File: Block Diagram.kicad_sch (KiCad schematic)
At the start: 0 parts

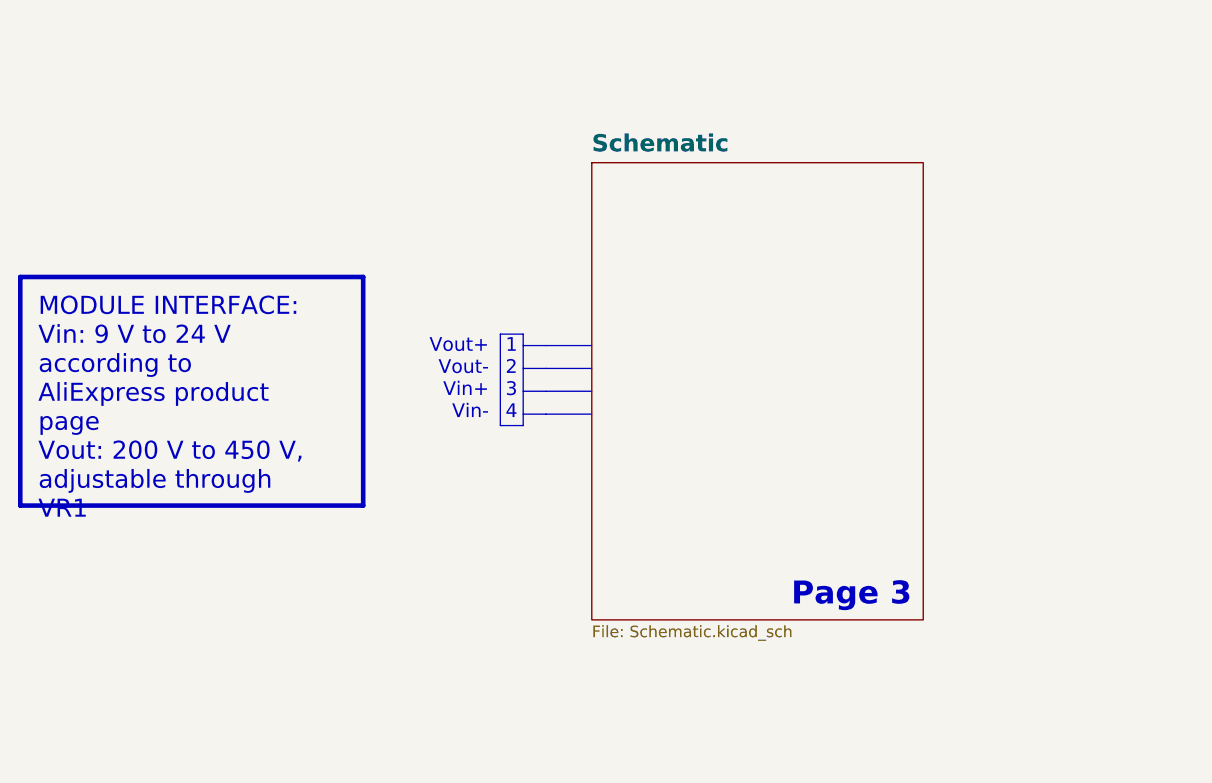
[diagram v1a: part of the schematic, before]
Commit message: changed grid origin pos.
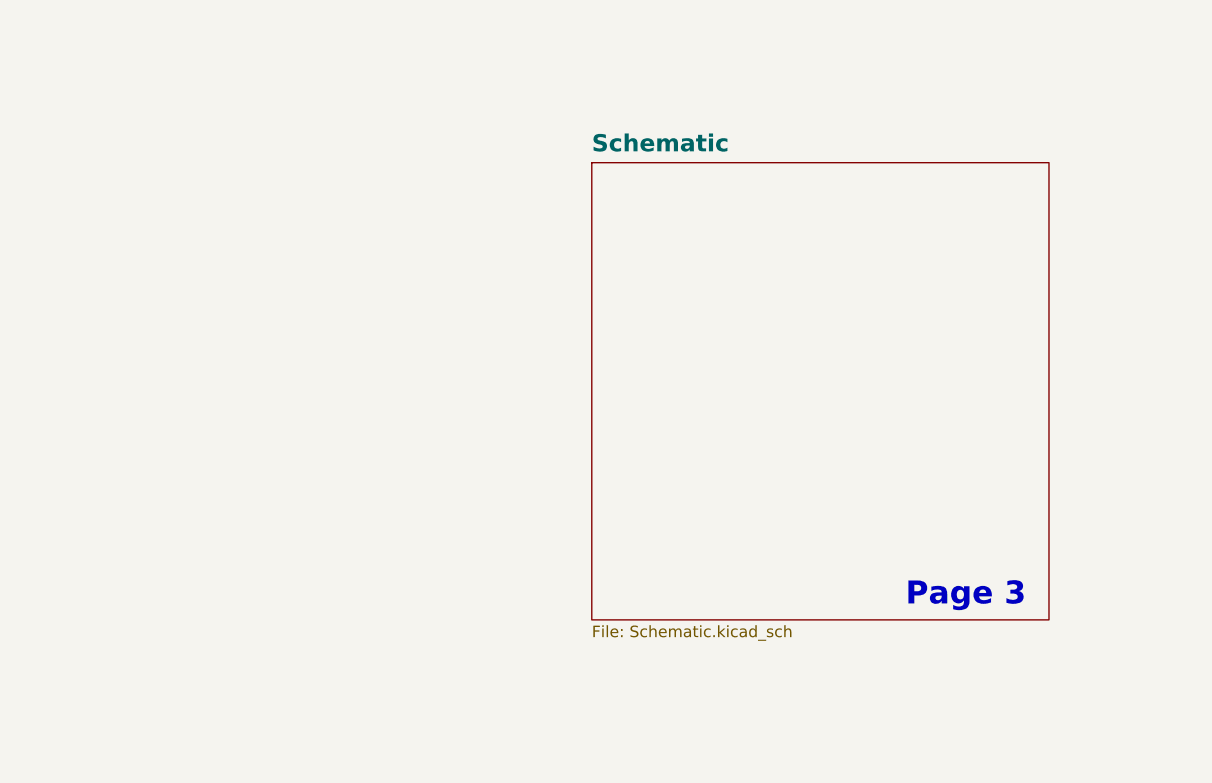
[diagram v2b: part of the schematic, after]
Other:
- note removed: "1 2 3 4"
- note removed: "Vout+ Vout- Vin+ Vin-"
